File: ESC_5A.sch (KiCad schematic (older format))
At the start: 16 parts, among them IC1 ATSAMD21E17D-AUT, IC2 AP2112K-3.3TRG1, J1 USB4105-GF-A, SW1 SW_Push

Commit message: adding driver
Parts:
- added C?: 270pF, symbol pspice:CAP
- added C?: 100uF, symbol pspice:CAP
- added C?: .1uF, symbol pspice:CAP
- added R4: 15k, symbol Device:R_US
- added R5, R? (x2): 10k, symbol Device:R_US
- added R?: 5.1k, symbol Device:R_US
- gave numbers to parts that had none: 1
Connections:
- net labels added: CTRL_1, CTRL_2, FB, LO, OSCM, PWR_IN, VCC_Driver
- wire segments 43 -> 80
- no-connect marks 4 -> 21

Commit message: EOD fri
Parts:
- added C11: .1uF, symbol pspice:CAP
- added R6: .1, symbol Device:R_US
- gave numbers to parts that had none: 6
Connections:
- net labels added: OUT+, OUT-, RS, TBLK
- wire segments 80 -> 97
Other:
- moved on the sheet: C10, C5, C6, C7, C8, C9, IC1, R4, R5, R7, R8, R9

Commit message: New Driver and rev_1 Schemetic. not including custom monitforing
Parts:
- removed C10: 100uF, symbol pspice:CAP
- removed C11, C9: .1uF, symbol pspice:CAP
- removed C8: 270pF, symbol pspice:CAP
- removed M1: TB67H401FTG,EL, QFN50P700X700X100-49N-D, symbol SamacSys_Parts:TB67H401FTG,EL
- removed R4: 15k, symbol Device:R_US
- removed R5, R8, R9: 10k, symbol Device:R_US
- removed R6: .1, symbol Device:R_US
- removed R7: 5.1k, symbol Device:R_US
- added C12, C13: 10uF, symbol pspice:CAP
- added D2: D_Schottky, symbol Device:D_Schottky
- added IC3: AP1501A-50K5G-13, AP1501A50K5G13, symbol SamacSys_Parts:AP1501A-50K5G-13
- added J2: Conn_01x03_Male, symbol Connector:Conn_01x03_Male
- added L1: 18uH, symbol Device:L
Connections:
- net labels added: HBMODE, INA1, INA2, INB1, INB2, LO1_MCU, LO2_MCU, PWMA, PWMB
- net labels removed: CTRL_1, CTRL_2, FB, LO, OSCM, OUT+, OUT-, RS, TBLK, VCC_Driver
- wire segments 97 -> 69
- no-connect marks 21 -> 5
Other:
- note added: "5V Output"
- note added: "5V Power Generation"
- note added: "MCU \n"
- moved on the sheet: C5, C6, C7, IC1

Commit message: leaving office
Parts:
- IC1: footprint QFP80P900X900X120-32N -> SamacSys_Parts:QFP80P900X900X120-32N
- IC2: footprint SOT95P282X130-5N -> SamacSys_Parts:SOT95P282X130-5N
- IC3: footprint AP1501A50K5G13 -> SamacSys_Parts:AP1501A50K5G13
- J1: footprint GCT_USB4105-GF-A -> USB4105-GF-A:GCT_USB4105-GF-A
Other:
- moved on the sheet: D2
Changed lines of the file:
@@
 encoding utf-8
 Sheet 1 2
-Title ""
+Title "ESC_5A"
 Date ""
-Rev ""
-Comp ""
+Rev "Rev One"
+Comp "50 Day"
 Comment1 ""
 Comment2 ""
@@
 F 0 "J1" H 2050 6267 50  0000 C CNN
 F 1 "USB4105-GF-A" H 2050 6176 50  0000 C CNN
-F 2 "GCT_USB4105-GF-A" H 2050 5600 50  0001 L BNN
+F 2 "USB4105-GF-A:GCT_USB4105-GF-A" H 2050 5600 50  0001 L BNN
 F 3 "" H 2050 5600 50  0001 L BNN
 F 4 "A3" H 2050 5600 50  0001 L BNN "PARTREV"
@@
 F 0 "IC2" H 5150 7165 50  0000 C CNN
 F 1 "AP2112K-3.3TRG1" H 5150 7074 50  0000 C CNN
-F 2 "SOT95P282X130-5N" H 5600 7000 50  0001 L CNN
+F 2 "SamacSys_Parts:SOT95P282X130-5N" H 5600 7000 50  0001 L CNN
 F 3 "" H 5600 6900 50  0001 L CNN
 F 4 "600mA 3.3V LDO Regulator Enable SOT23-5 DiodesZetex AP2112K-3.3TRG1, LDO Voltage Regulator, 3.3 V +/-1.5%, 2.5  6 Vin, 5-Pin SOT-23" H 5600 6800 50  0001 L CNN "Description"
@@
 F 0 "IC1" H 10094 3896 50  0000 L CNN
 F 1 "ATSAMD21E17D-AUT" H 10094 3805 50  0000 L CNN
-F 2 "QFP80P900X900X120-32N" H 9900 4750 50  0001 L CNN
+F 2 "SamacSys_Parts:QFP80P900X900X120-32N" H 9900 4750 50  0001 L CNN
 F 3 "https://componentsearchengine.com/Datasheets/1/ATSAMD21E17D-AUT.pdf" H 9900 4650 50  0001 L CNN
 F 4 "ARM Microcontrollers - MCU 32TQFP IND TEMP, GREEN,1.6-3.6V,48MHz" H 9900 4550 50  0001 L CNN "Description"
@@
 Text GLabel 1650 6750 1    50   Input ~ 0
 NRST
-Text GLabel 9650 3350 1    50   Input ~ 0
+Text GLabel 9650 3300 1    50   Input ~ 0
 NRST
 $Comp
@@
 Wire Wire Line
 	8750 6050 8750 6150
-Text GLabel 10050 4150 2    50   Input ~ 0
+Text GLabel 10100 4150 2    50   Input ~ 0
 D+
-Text GLabel 10050 4250 2    50   Input ~ 0
+Text GLabel 10100 4250 2    50   Input ~ 0
 D-
 Wire Wire Line
@@
 F 0 "IC3" H 5700 5015 50  0000 C CNN
 F 1 "AP1501A-50K5G-13" H 5700 4924 50  0000 C CNN
-F 2 "AP1501A50K5G13" H 6200 4850 50  0001 L CNN
+F 2 "SamacSys_Parts:AP1501A50K5G13" H 6200 4850 50  0001 L CNN
 F 3 "https://www.arrow.com/en/products/ap1501a-50k5g-13/diodes-incorporated" H 6200 4750 50  0001 L CNN
 F 4 "Switching Voltage Regulators BUCK CONV PWM 150KHz 5A 4.5-40V 1.23V" H 6200 4650 50  0001 L CNN "Description"
@@
 	4900 4850 4900 5650
 Wire Wire Line
-	4900 5650 5050 5650
-Wire Wire Line
 	4900 4850 5050 4850
 Wire Wire Line
@@
 L Device:D_Schottky D2
 U 1 1 60D69172
-P 5050 5800
-F 0 "D2" V 5004 5880 50  0000 L CNN
-F 1 "D_Schottky" V 5095 5880 50  0000 L CNN
-F 2 "" H 5050 5800 50  0001 C CNN
-F 3 "~" H 5050 5800 50  0001 C CNN
-	1    5050 5800
+P 5050 5900
+F 0 "D2" V 5004 5980 50  0000 L CNN
+F 1 "D_Schottky" V 5095 5980 50  0000 L CNN
+F 2 "" H 5050 5900 50  0001 C CNN
+F 3 "~" H 5050 5900 50  0001 C CNN
+	1    5050 5900
 	0    1    1    0
 $EndComp
-Connection ~ 5050 5650
-Wire Wire Line
-	5050 5650 5300 5650
 Wire Wire Line
 	5600 5650 5800 5650
@@
 Wire Wire Line
 	4650 5150 4650 6150
-Wire Wire Line
-	4650 6150 5050 6150
 Connection ~ 4650 5150
 Wire Wire Line
 	4650 5150 4850 5150
-Wire Wire Line
-	5050 5950 5050 6150
-Connection ~ 5050 6150
-Wire Wire Line
-	5050 6150 5250 6150
 Wire Wire Line
 	5250 6150 5250 6200
@@
 F1 "Motor_Driver.sch" 50
 $EndSheet
-Text GLabel 8750 4150 0    50   Input ~ 0
+Text GLabel 8700 4150 0    50   Input ~ 0
 LO1_MCU
-Text GLabel 8750 4250 0    50   Input ~ 0
+Text GLabel 8700 4250 0    50   Input ~ 0
 LO2_MCU
-Text GLabel 8750 4350 0    50   Input ~ 0
+Text GLabel 8700 4350 0    50   Input ~ 0
 PWMA
-Text GLabel 8750 4450 0    50   Input ~ 0
+Text GLabel 8700 4450 0    50   Input ~ 0
 PWMB
-Text GLabel 8750 4750 0    50   Input ~ 0
+Text GLabel 8700 4750 0    50   Input ~ 0
 INB1
-Text GLabel 8750 4850 0    50   Input ~ 0
+Text GLabel 8700 4850 0    50   Input ~ 0
 INB2
-Text GLabel 8750 4550 0    50   Input ~ 0
+Text GLabel 8700 4550 0    50   Input ~ 0
 INA1
-Text GLabel 8750 4650 0    50   Input ~ 0
+Text GLabel 8700 4650 0    50   Input ~ 0
 INA2
-Text GLabel 9250 5550 3    50   Input ~ 0
+Text GLabel 9250 5650 3    50   Input ~ 0
 HBMODE
 Wire Wire Line
@@
 Text Notes 7000 2950 0    50   ~ 0
 MCU \n
+Wire Wire Line
+	9250 5650 9250 5550
+Wire Wire Line
+	4650 6150 5050 6150
+Wire Wire Line
+	4900 5650 5050 5650
+Wire Wire Line
+	5050 5750 5050 5650
+Connection ~ 5050 5650
+Wire Wire Line
+	5050 5650 5300 5650
+Wire Wire Line
+	5050 6050 5050 6150
+Connection ~ 5050 6150
+Wire Wire Line
+	5050 6150 5250 6150
+Wire Wire Line
+	8750 4150 8700 4150
+Wire Wire Line
+	8750 4250 8700 4250
+Wire Wire Line
+	8750 4350 8700 4350
+Wire Wire Line
+	8750 4450 8700 4450
+Wire Wire Line
+	8750 4550 8700 4550
+Wire Wire Line
+	8750 4650 8700 4650
+Wire Wire Line
+	8750 4750 8700 4750
+Wire Wire Line
+	8750 4850 8700 4850
+Wire Wire Line
+	10050 4150 10100 4150
+Wire Wire Line
+	10050 4250 10100 4250
+Wire Wire Line
+	9650 3300 9650 3350
 $EndSCHEMATC

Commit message: Schematic Rev_One Done pre review
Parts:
- removed C1, C12, C13, C2: 10uF, symbol pspice:CAP
- removed C3, C5: 1uF, symbol pspice:CAP
- removed C4, C6, C7: .1uF, symbol pspice:CAP
- removed D2: D_Schottky, symbol Device:D_Schottky
- removed IC2: AP2112K-3.3TRG1, SamacSys_Parts:SOT95P282X130-5N, symbol SamacSys_Parts:AP2112K-3.3TRG1
- removed L1: 18uH, symbol Device:L
- removed SW1: SW_Push, symbol Switch:SW_Push
- added C1, C8, C9: .1uF, SamacSys_Parts:CAPC0603X33N, symbol SamacSys_Parts:GRM033R61C104KE84D
- added C2, C5, C6: 10uF, SamacSys_Parts:C1608_Commercial, symbol SamacSys_Parts:C1608X5R1C106M080AB
- added C3: 10uF, SamacSys_Parts:CAPC3216X180N, symbol SamacSys_Parts:GRT31CR61H106KE01L
- added C4, C7: 1uF, SamacSys_Parts:CAPC1005X55N, symbol SamacSys_Parts:GRM155C81C105KE11J
- added D2: B340AE-13, SamacSys_Parts:DIOM5226X240N, symbol SamacSys_Parts:B340AE-13
- added IC1: AT25M02-SSHM-T, SamacSys_Parts:SOIC127P600X175-8N, symbol SamacSys_Parts:AT25M02-SSHM-T
- added IC2: AP2112M-3.3TRG1, SamacSys_Parts:SOIC127P600X170-8N, symbol SamacSys_Parts:AP2112M-3.3TRG1
- added L1: 33uH, SamacSys_Parts:SRR1260-150M, symbol SamacSys_Parts:SRR1260-330M
- added R4: 5.1k, Resistor_SMD:R_0402_1005Metric, symbol Device:R_US
- added S1: LL3301NF065QG, SamacSys_Parts:LL3301NF065QG, symbol SamacSys_Parts:LL3301NF065QG
- J2: footprint (none) -> Connector_PinHeader_2.54mm:PinHeader_1x03_P2.54mm_Vertical
- R1: footprint (none) -> Resistor_SMD:R_0402_1005Metric
- R2: renamed from R3; footprint (none) -> Resistor_SMD:R_0402_1005Metric
- R3: renamed from R2; footprint (none) -> Resistor_SMD:R_0402_1005Metric
- renumbered IC1 to IC4
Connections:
- net +3V3: now also C2.1, C4.1, IC1.3 (~WP), IC1.7 (~HOLD), IC1.8 (VCC), IC2.1 (VOUT), R4.1
- net +5V: now also C5.1, C6.1, IC2.5 (EN), IC2.8 (VIN), L1.2
- net GND: now also C1.1, C2.2, C3.2, C4.2, C5.2, C6.2, C7.2, C8.1, C9.1, D2.2, IC1.4 (GND), IC2.6 (GND_1), IC2.7 (GND_2), S1.1, S1.3
- net HBMODE: now also IC4.25 (PA27); no longer IC4.11 (PA08)
- net INA1: now also IC4.12 (PA09); no longer IC4.5 (PA04)
- net INA2: now also IC4.13 (PA10); no longer IC4.6 (PA05)
- net INB1: now also IC4.14 (PA11); no longer IC4.7 (PA06)
- net INB2: now also IC4.15 (PA14); no longer IC4.8 (PA07)
- net NRST: now also C1.2, S1.2, S1.4
- net PWMA: now also IC4.17 (PA16); no longer IC4.3 (PA02)
- net PWMB: now also IC4.18 (PA17); no longer IC4.4 (PA03)
- net PWR_IN: now also C3.1
- net RGB_DATA: now also IC4.19 (PA18)
- net RGB_PWR: now also IC4.16 (PA15)
- net MISO_EEPROM: now reaches IC4.20 (PA19)
- net MISO_EEPROM: now also IC1.2 (SO)
- net SCK_EEPROM: now reaches IC4.21 (PA22)
- net SCK_EEPROM: now also IC1.6 (SCK)
- net MOSI_EEPROM: now reaches IC4.22 (PA23)
- net MOSI_EEPROM: now also IC1.5 (SI)
- net at IC4.29 (VDDCORE): now also C7.1
- net at IC4.30 (VDDIN): now also C8.2
- net at IC4.9 (VDDANA): now also C9.2
- net at IC3.2 (OUTPUT): now also D2.1, L1.1
- new net ADC_1: IC4.7 (PA06)
- new net ADC_2: IC4.8 (PA07)
- new net ADC_3: IC4.6 (PA05)
- new net ADC_MUX_GND: IC4.3 (PA02)
- new net ADC_VREFA: IC4.4 (PA03)
- new net ADC_VREFB: IC4.5 (PA04)
- new net CS_EEPROM: IC1.1 (~CS), IC4.11 (PA08), R4.2
- no-connect marks 5 -> 7
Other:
- note added: "EEPROM"
- moved on the sheet: IC3, J1, R1, R2, R3

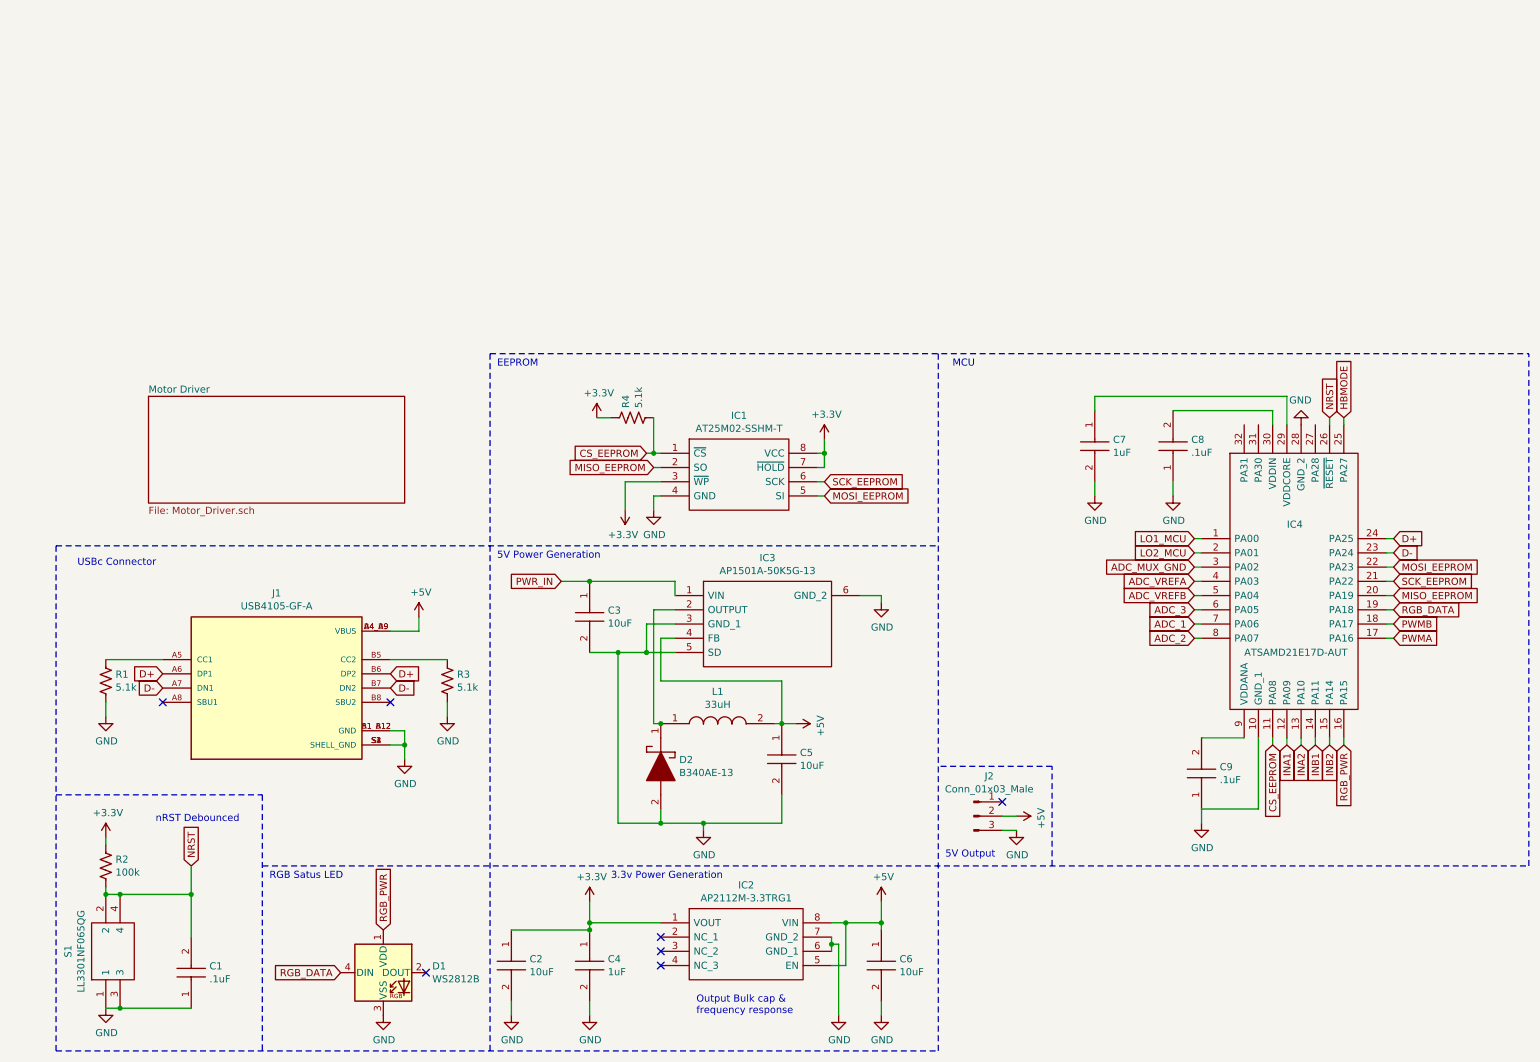
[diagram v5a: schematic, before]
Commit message: Layout Rev_One done need to revise to shrink board
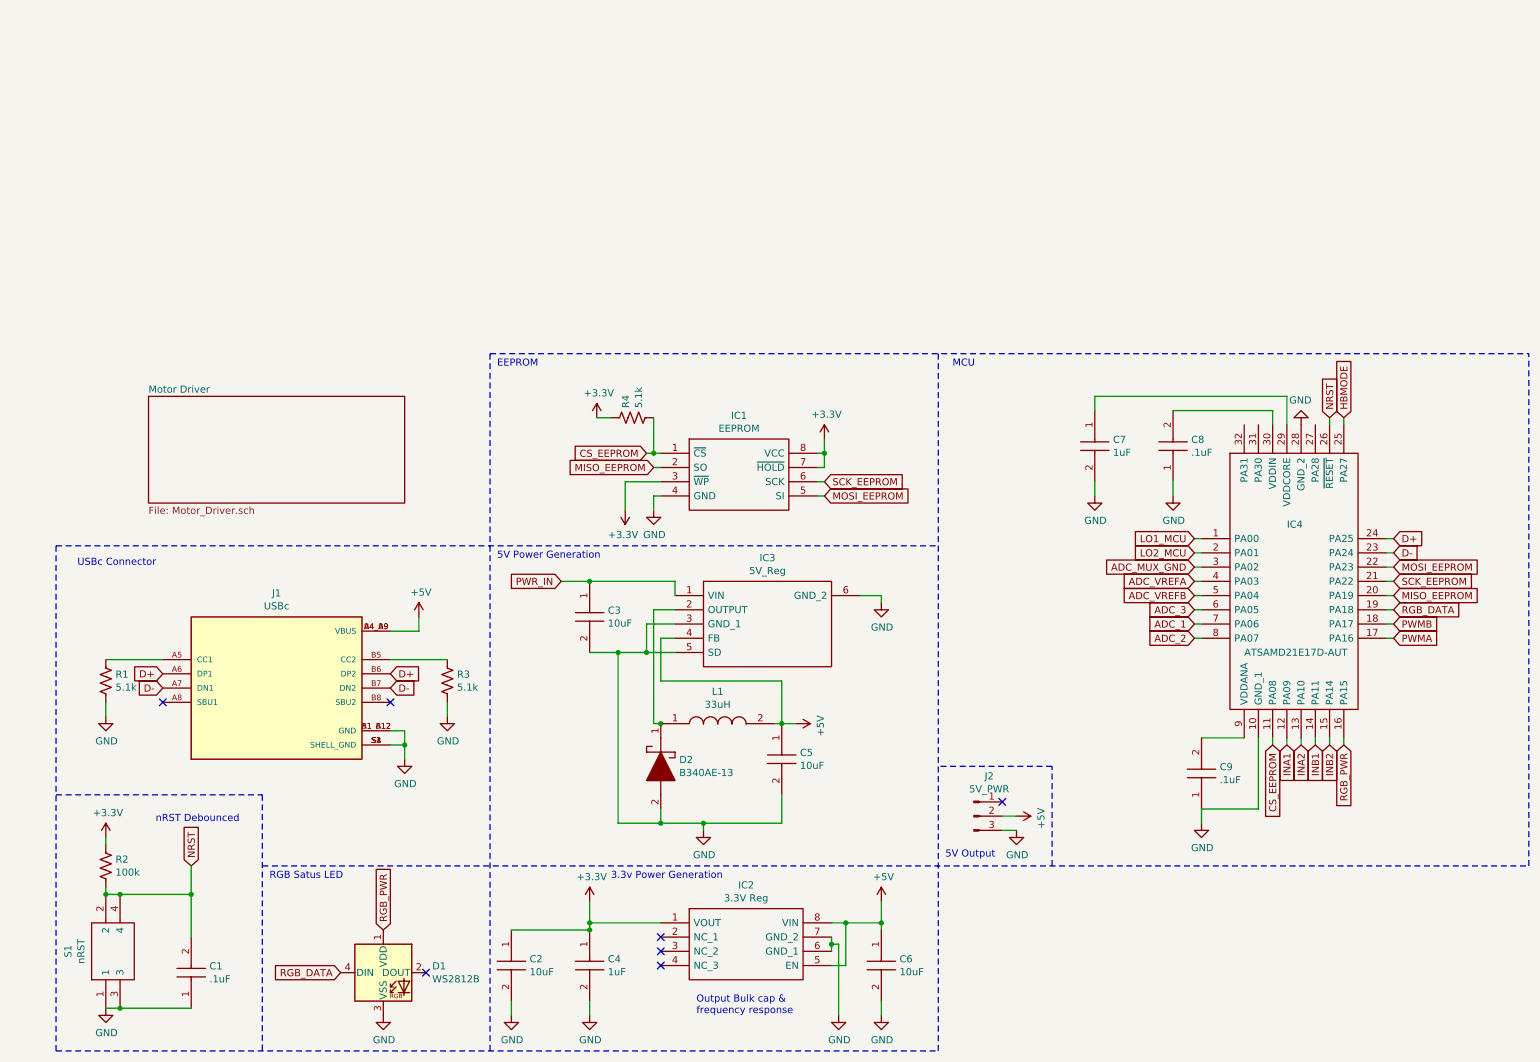
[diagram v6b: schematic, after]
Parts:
- IC1: value AT25M02-SSHM-T -> EEPROM
- IC2: value AP2112M-3.3TRG1 -> 3.3V Reg
- IC3: value AP1501A-50K5G-13 -> 5V_Reg
- J1: value USB4105-GF-A -> USBc
- J2: value Conn_01x03_Male -> 5V_PWR
- S1: value LL3301NF065QG -> nRST
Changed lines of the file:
@@
 P 2250 5200
 F 0 "J1" H 2250 5867 50  0000 C CNN
-F 1 "USB4105-GF-A" H 2250 5776 50  0000 C CNN
+F 1 "USBc" H 2250 5776 50  0000 C CNN
 F 2 "USB4105-GF-A:GCT_USB4105-GF-A" H 2250 5200 50  0001 L BNN
 F 3 "" H 2250 5200 50  0001 L BNN
@@
 P 5050 4550
 F 0 "IC3" H 5700 4815 50  0000 C CNN
-F 1 "AP1501A-50K5G-13" H 5700 4724 50  0000 C CNN
+F 1 "5V_Reg" H 5700 4724 50  0000 C CNN
 F 2 "SamacSys_Parts:AP1501A50K5G13" H 6200 4650 50  0001 L CNN
 F 3 "https://www.arrow.com/en/products/ap1501a-50k5g-13/diodes-incorporated" H 6200 4550 50  0001 L CNN
@@
 P 7150 6100
 F 0 "J2" H 7258 6381 50  0000 C CNN
-F 1 "Conn_01x03_Male" H 7258 6290 50  0000 C CNN
+F 1 "5V_PWR" H 7258 6290 50  0000 C CNN
 F 2 "Connector_PinHeader_2.54mm:PinHeader_1x03_P2.54mm_Vertical" H 7150 6100 50  0001 C CNN
 F 3 "~" H 7150 6100 50  0001 C CNN
@@
 P 4950 6850
 F 0 "IC2" H 5550 7115 50  0000 C CNN
-F 1 "AP2112M-3.3TRG1" H 5550 7024 50  0000 C CNN
+F 1 "3.3V Reg" H 5550 7024 50  0000 C CNN
 F 2 "SamacSys_Parts:SOIC127P600X170-8N" H 6000 6950 50  0001 L CNN
 F 3 "https://www.diodes.com/assets/Datasheets/AP2112.pdf" H 6000 6850 50  0001 L CNN
@@
 P 4950 3550
 F 0 "IC1" H 5500 3815 50  0000 C CNN
-F 1 "AT25M02-SSHM-T" H 5500 3724 50  0000 C CNN
+F 1 "EEPROM" H 5500 3724 50  0000 C CNN
 F 2 "SamacSys_Parts:SOIC127P600X175-8N" H 5900 3650 50  0001 L CNN
 F 3 "http://ww1.microchip.com/downloads/en/DeviceDoc/Atmel-8832C-SEEPROM-AT25M02-Datasheet.pdf" H 5900 3550 50  0001 L CNN
@@
 P 1050 7450
 F 0 "S1" H 1450 7715 50  0000 C CNN
-F 1 "LL3301NF065QG" H 1450 7624 50  0000 C CNN
+F 1 "nRST" H 1450 7624 50  0000 C CNN
 F 2 "SamacSys_Parts:LL3301NF065QG" H 1700 7550 50  0001 L CNN
 F 3 "http://spec_sheets.e-switch.com/specs/P090002.pdf" H 1700 7450 50  0001 L CNN

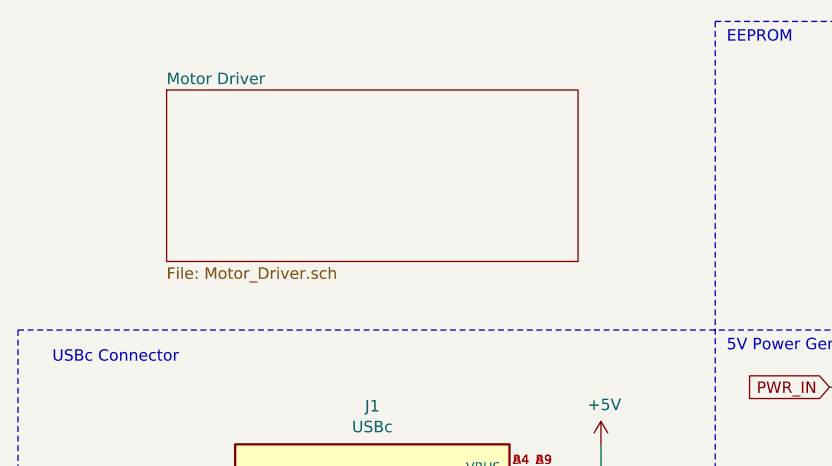
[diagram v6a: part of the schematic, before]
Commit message: Added M2 mounting holes and cleaned solder mask
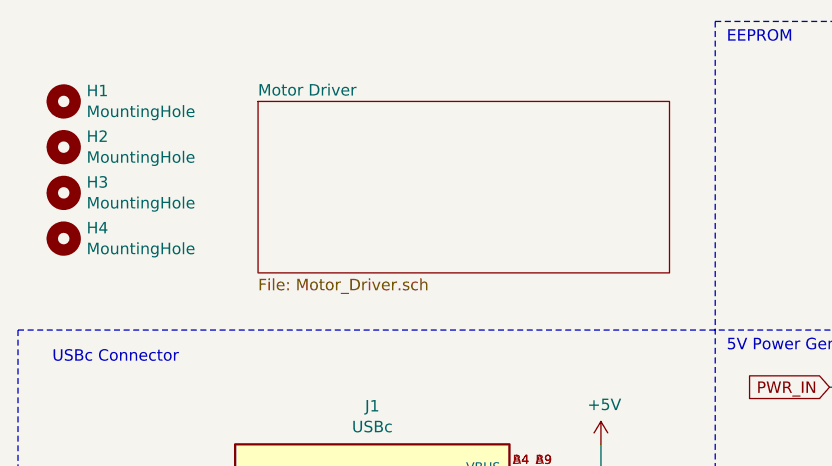
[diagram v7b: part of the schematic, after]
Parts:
- added H1, H2, H3, H4: MountingHole, MountingHole:MountingHole_2.2mm_M2, symbol Mechanical:MountingHole
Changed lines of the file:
@@
 5V Output
 $Sheet
-S 1350 3150 1800 750
+S 1750 3200 1800 750
 U 60E06626
 F0 "Motor Driver" 50
@@
 Wire Notes Line
 	2150 5950 2150 7750
+$Comp
+L Mechanical:MountingHole H4
+U 1 1 60F87E36
+P 900 3800
+F 0 "H4" H 1000 3846 50  0000 L CNN
+F 1 "MountingHole" H 1000 3755 50  0000 L CNN
+F 2 "MountingHole:MountingHole_2.2mm_M2" H 900 3800 50  0001 C CNN
+F 3 "~" H 900 3800 50  0001 C CNN
+	1    900  3800
+	1    0    0    -1
+$EndComp
+$Comp
+L Mechanical:MountingHole H3
+U 1 1 60F8848E
+P 900 3600
+F 0 "H3" H 1000 3646 50  0000 L CNN
+F 1 "MountingHole" H 1000 3555 50  0000 L CNN
+F 2 "MountingHole:MountingHole_2.2mm_M2" H 900 3600 50  0001 C CNN
+F 3 "~" H 900 3600 50  0001 C CNN
+	1    900  3600
+	1    0    0    -1
+$EndComp
+$Comp
+L Mechanical:MountingHole H2
+U 1 1 60F8BEE8
+P 900 3400
+F 0 "H2" H 1000 3446 50  0000 L CNN
+F 1 "MountingHole" H 1000 3355 50  0000 L CNN
+F 2 "MountingHole:MountingHole_2.2mm_M2" H 900 3400 50  0001 C CNN
+F 3 "~" H 900 3400 50  0001 C CNN
+	1    900  3400
+	1    0    0    -1
+$EndComp
+$Comp
+L Mechanical:MountingHole H1
+U 1 1 60F8F7AC
+P 900 3200
+F 0 "H1" H 1000 3246 50  0000 L CNN
+F 1 "MountingHole" H 1000 3155 50  0000 L CNN
+F 2 "MountingHole:MountingHole_2.2mm_M2" H 900 3200 50  0001 C CNN
+F 3 "~" H 900 3200 50  0001 C CNN
+	1    900  3200
+	1    0    0    -1
+$EndComp
 $EndSCHEMATC
